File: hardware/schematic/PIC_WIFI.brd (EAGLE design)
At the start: 111.5 x 26.4 mm, 63 parts, among them J3 M40, J4 M40, J7 USB-A-S, Q1 8MHz, Q2 32.768KHz, U1 PIC32MX460F512L TQFP100, U2 3.3V, U3 5V

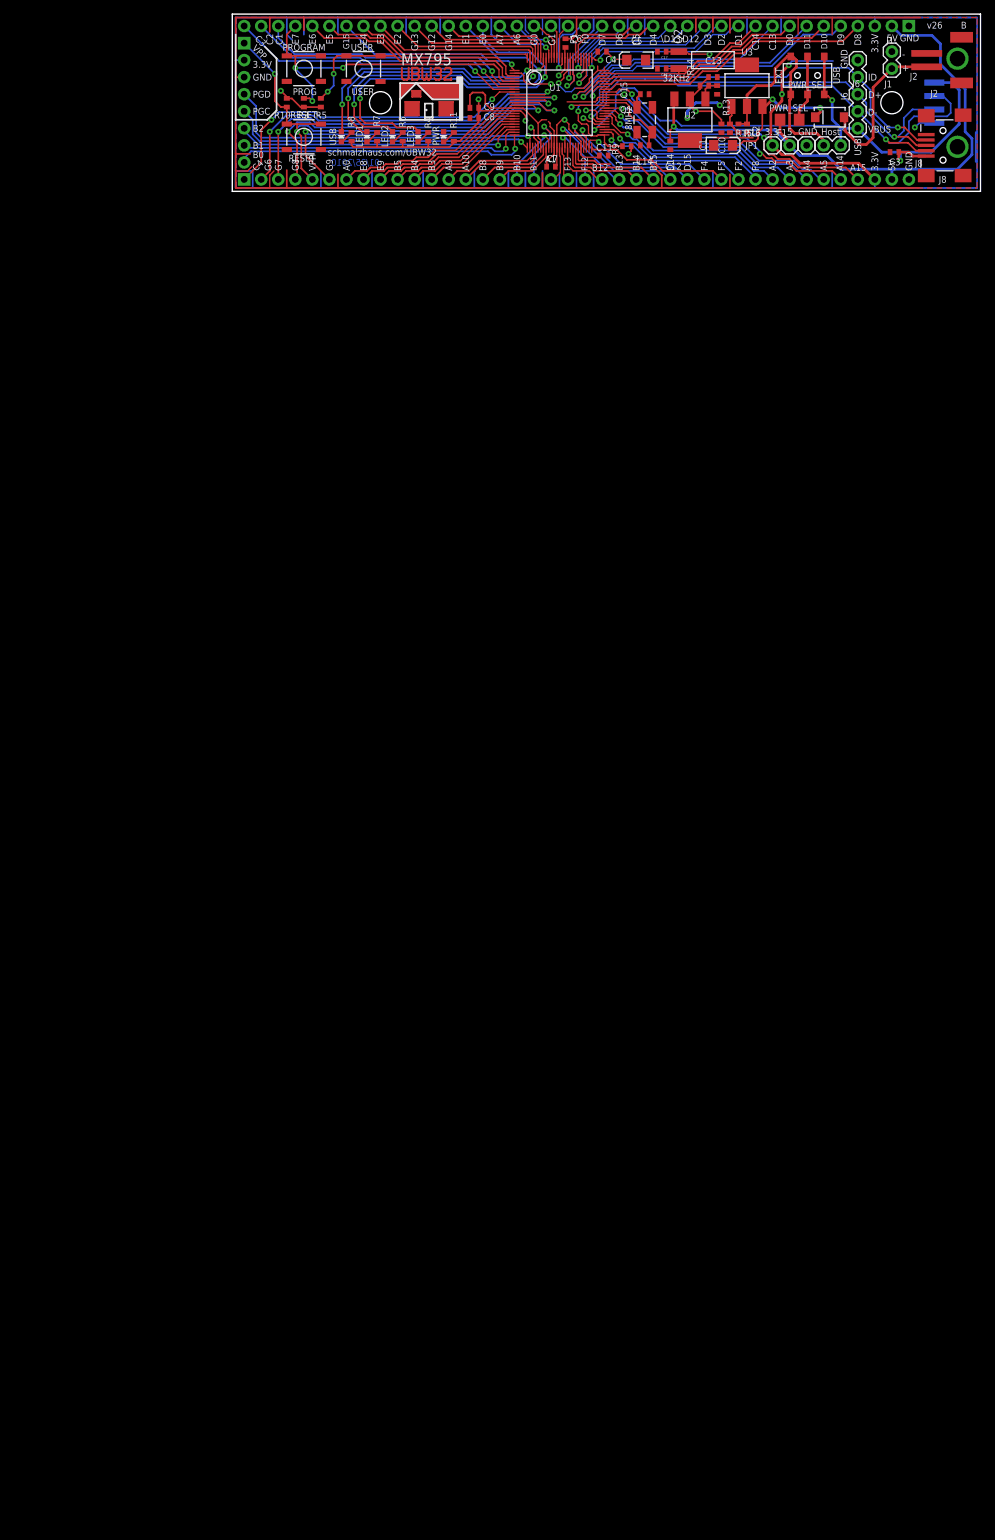
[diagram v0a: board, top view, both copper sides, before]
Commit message: First revision of dev board.  Fixed duplicate pin in waterworx.sch
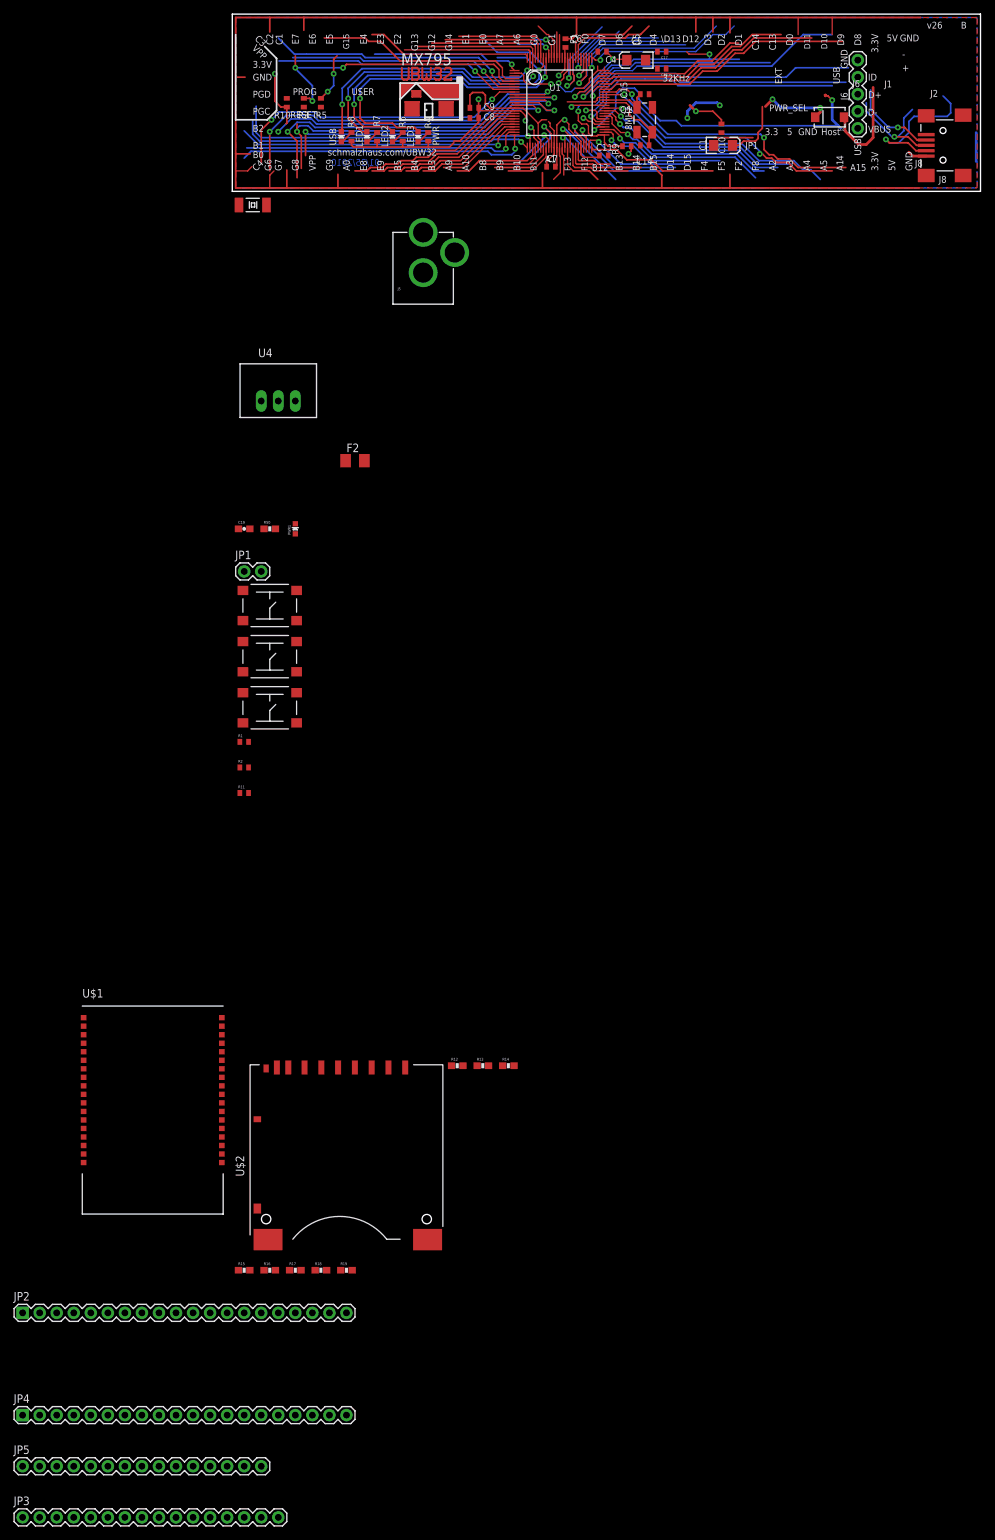
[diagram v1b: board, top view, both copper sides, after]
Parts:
- removed 3.3, 5, GND: M01PTH, SparkFun-12-01-09:1X01
- removed C12, C13: 1uF, SparkFun02-20-08:C0402
- removed C2, C3: 1uF, SparkFun:C0402
- removed F1: 250mA PTC Fuse, resistor:R1206
- removed J1: (no value), SparkFun-12-01-09:1X02
- removed J2: (no value), SparkFun:S2B-PH
- removed J3, J4: M40, SchmalzHaus:1X40
- removed J7: USB-A-S, SparkFun02-20-08:USB-A-S
- removed PROGRAM, USER: (no value), SparkFun02-20-08:TACTILE_SWITCH_SMD
- removed PWR: BLUE, SparkFun:LED-0603
- removed PWR_SEL: AYZ0202, SparkFun02-20-08:AYZ0202
- removed U$4: LOGO-SFENEW, SparkFun02-20-08:SFE-NEW-WEBLOGO
- removed U$6, U$7: STAND-OFF, SparkFun02-20-08:STAND-OFF
- removed U2: 3.3V, SparkFun:SOT223
- removed U3: 5V, SparkFun:SOT223
- added C19: 1uF, SparkFun-Passives:0603-CAP
- added F2: 500mA PTC Fuse, resistor:M1206
- added JP2, JP4: M20, SparkFun-Connectors:1X20
- added JP3: M16PTH, SparkFun-Connectors:1X16
- added JP5: M15, SparkFun-Connectors:1X15
- added PWR1: BLUE, SparkFun:LED-0603
- added R1, R2: 4.7K, SparkFun:C0402
- added R12, R17, R18, R19: 4.7K, SparkFun-Passives:0603-RES
- added R50: 330, SparkFun-Passives:0603-RES
- added U$1: MRF24WB0MA, lizardworx:SMD_MRF
- added U$2: SD_CARD_SOCKETALPS, lizardworx:SD_ALPS
- added U4: RECOM_X.X_REG78XX, lizardworx:RECOM
- added USER1, USER2: (no value), lizardworx:SWITCH-OMRON
- J5: value (none) -> POWER_JACKPTH; device SchmalzHaus:1X08 -> lizardworx:POWER_JACK_PTH
- JP1: device SparkFun-12-01-09:1X02 -> SparkFun-Connectors:1X02
- Q2: device SchmalzHaus:CRYSTAL-32KHZ-SMD -> lizardworx:CRYSTAL-SMD-4X2
- R10, R3, R5: value 10K -> 4.7K
- R11: value 330 -> 4.7K
- R13: value 390 -> 4.7K; device SparkFun:C0402 -> SparkFun-Passives:0603-RES
- R14, R16: value 240 -> 4.7K; device SparkFun:C0402 -> SparkFun-Passives:0603-RES
- R15: value 715 -> 4.7K; device SparkFun:C0402 -> SparkFun-Passives:0603-RES
- RESET: device SparkFun02-20-08:TACTILE_SWITCH_SMD -> lizardworx:SWITCH-OMRON
- moved R15 184.9 mm to (1.27, -161.3), turned to 0 degrees
- moved R16 184.0 mm to (5.08, -161.3), turned to 0 degrees
- moved R13 149.6 mm to (36.8, -130.8), turned to 0 degrees
- moved R14 148.9 mm to (40.6, -130.8)
- moved JP1 107.2 mm to (1.27, -57.1)
- moved R11 102.7 mm to (1.27, -90.2), turned to 0 degrees
- moved RESET 85.2 mm to (5.08, -77.5), turned to 0 degrees
- moved Q2 67.1 mm to (2.54, -2.54), turned to 0 degrees
- moved J5 49.7 mm to (27.9, -20.3), turned to 0 degrees
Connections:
- removed net 5V: 5.1, C12.1, F1.2, J3.2, J4.39, U2.3
- removed net 5V_ALT: C2.1, JP1.1, PWR_SEL.1, PWR_SEL.4, R16.1, U3.2
- removed net N$6: PWR.A, R11.1
- removed net RA3: J4.33, U1.59
- removed net RC4: J4.1, U1.9
- removed net RD0: J3.8, U1.72
- removed net RD10: J3.6, U1.70
- removed net RE8: J4.8, U1.18
- removed net RF0: J3.20, U1.87
- removed net RF1: J3.21, U1.88
- removed net RG12: J3.29, U1.96
- removed net RG13: J3.30, U1.97
- removed net RG14: J3.28, U1.95
- removed net RG6: J4.2, U1.10
- removed net RG7: J4.3, U1.11
- removed net RG8: J4.4, U1.12
- new net N$10: R18.1, R19.1
- new net N$19: PWR1.A, R50.1
- new net N$24: C19.1, F2.2, U4.VOUT
- new net N$5: R15.2, U$1.4
- new net SD_CD: JP2.9, U$2.CD, U1.96
- new net SD_CK: JP4.1, U$2.5, U1.10
- new net SD_CS: JP2.8, R18.2, U$2.1, U1.95
- new net SD_DI: JP4.3, U$2.2, U1.12
- new net SD_DO: JP4.2, U$2.7, U1.11
- new net SD_WP: JP2.10, U$2.WP, U1.97
- new net WF_CK: R13.1, U$1.34, U1.70
- new net WF_CS: U$1.23, U1.59
- new net WF_DI: R12.1, U$1.35, U1.72
- new net WF_DO: U$1.32, U1.9
- new net WF_HIBERNATE: U$1.20, U1.88
- new net WF_INT: R14.1, U$1.33, U1.18
- new net WF_RESET: R16.1, U$1.7, U1.87
- new net WF_WP: R17.2, U$1.16
- net 3.3V: now also F2.1, J6.2, JP3.2, JP5.14, R1.2, R12.2, R13.2, R14.2, R15.1, R16.2, R19.2, R2.2, R50.2, U$1.17, U$1.29, U$2.4; no longer 3.3.1, C13.1, J3.3, J4.38, J5.2, R10.1, R14.1, R3.1, R5.1, U2.2
- net D+: no longer J6.3, J7.D+
- net D-: no longer J6.2, J7.D-
- net GND: now also C19.2, J5.GND, J5.GNDBREAK, J6.3, JP1.2, JP3.1, JP5.15, PWR1.C, R17.1, U$1.1, U$1.10, U$1.18, U$1.19, U$1.25, U$1.28, U$1.30, U$1.36, U$2.12, U$2.3, U$2.6, U$2.VSS, U4.GND, USER1.1, USER1.2, USER2.1, USER2.2; no longer C12.2, C13.2, C2.2, C3.2, GND.1, J1.1, J2.1, J3.1, J4.40, J5.3, J6.5, J7.GND, PROGRAM.1, PROGRAM.2, PWR.C, R13.1, R15.1, USER.1, USER.2
- net N$1: now also R1.1, R10.1; no longer D1.A, J1.2, J2.2
- net N$2: now also D1.A, J5.PWR, JP1.1; no longer F1.1, PWR_SEL.2, PWR_SEL.5
- net N$3: now also R2.1, R5.1; no longer R13.2, R14.2, U2.1
- net N$4: now also R11.1, R3.1; no longer R15.2, R16.2, U3.1
- net PGC: now also J6.5; no longer J5.5
- net PGD: now also J6.4; no longer J5.4
- net RA0: now also JP4.5; no longer J4.7
- net RA1: now also JP4.16; no longer J4.19
- net RA10: now also JP4.11; no longer J4.14
- net RA14: now also JP5.12; no longer J4.36
- net RA15: now also JP5.13; no longer J4.37
- net RA2: now also JP5.9; no longer J4.32
- net RA4: now also JP5.10; no longer J4.34
- net RA5: now also JP5.11; no longer J4.35
- net RA6: now also JP2.4; no longer J3.24
- net RA7: now also JP2.5; no longer J3.25
- net RA9: now also JP4.10; no longer J4.13
- net RB0: no longer J5.8
- net RB1: no longer J5.7
- net RB10: now also JP4.14; no longer J4.17
- net RB11: now also JP4.15; no longer J4.18
- net RB12: now also JP4.19; no longer J4.22
- net RB13: now also JP4.20; no longer J4.23
- net RB14: now also JP5.1; no longer J4.24
- net RB15: now also JP5.2; no longer J4.25
- net RB2: no longer J5.6
- net RB3: now also JP4.9; no longer J4.12
- net RB4: now also JP4.8; no longer J4.11
- net RB5: now also JP4.7; no longer J4.10
- net RB8: now also JP4.12; no longer J4.15
- net RB9: now also JP4.13; no longer J4.16
- net RC1: now also JP2.18; no longer J3.38
- net RC13: now also JP3.6, Q2.P$2; no longer J3.9, Q2.X1
- net RC14: now also JP3.7, Q2.P$1; no longer J3.10, Q2.X2
- net RC2: now also JP2.19; no longer J3.39
- net RC3: now also JP2.20; no longer J3.40
- net RD1: now also JP3.8; no longer J3.11
- net RD11: now also JP3.5; no longer J3.7
- net RD12: now also JP3.11; no longer J3.14
- net RD13: now also JP3.12; no longer J3.15
- net RD14: now also JP5.3; no longer J4.26
- net RD15: now also JP5.4; no longer J4.27
- net RD2: now also JP3.9; no longer J3.12
- net RD3: now also JP3.10; no longer J3.13
- net RD4: now also JP3.13; no longer J3.16
- net RD5: now also JP3.14; no longer J3.17
- net RD6: now also JP3.15; no longer J3.18
- net RD7: now also JP2.1; no longer J3.19
- net RD8: now also JP3.3; no longer J3.4
- net RD9: now also JP3.4; no longer J3.5
- net RE0: now also JP2.6; no longer J3.26
- net RE1: now also JP2.7; no longer J3.27
- net RE2: now also JP2.11; no longer J3.31
- net RE3: now also JP2.12; no longer J3.32
- net RE4: now also JP2.13; no longer J3.33
- net RE5: now also JP2.15; no longer J3.35
- net RE6: now also JP2.16, USER2.3, USER2.4; no longer J3.36, USER.3, USER.4
- net RE7: now also JP2.17, USER1.3, USER1.4; no longer J3.37, PROGRAM.3, PROGRAM.4
- net RE9: now also JP4.6; no longer J4.9
- net RF12: now also JP4.18; no longer J4.21
- net RF13: now also JP4.17; no longer J4.20
- net RF2: now also JP5.7; no longer J4.30
- net RF4: now also JP5.5; no longer J4.28
- net RF5: now also JP5.6; no longer J4.29
- net RF8: now also JP5.8; no longer J4.31
- net RG0: now also JP2.3; no longer J3.23
- net RG1: now also JP2.2; no longer J3.22
- net RG15: now also JP2.14; no longer J3.34
- net RG9: now also JP4.4; no longer J4.6
- net USBID: no longer J6.4
- net VBUS: no longer C3.1, J6.1, J7.VBUS, JP1.2, PWR_SEL.3, PWR_SEL.6
- net VIN_RAW: now also U4.VIN; no longer U3.3
- net VPP: now also J6.1; no longer J4.5, J5.1
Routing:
- net 3.3V: track 486.2 -> 87.3 mm, vias 13 -> 10
- net 5V: track 87.3 -> 0.00 mm, vias 1 -> 0
- net RG6: track 57.3 -> 0.00 mm, vias 2 -> 0
- net RG7: track 56.9 -> 0.00 mm, vias 2 -> 0
- net SD_CK: track 0.00 -> 55.5 mm, vias 0 -> 2
- net RG8: track 54.6 -> 0.00 mm, vias 2 -> 0
- net SD_DI: track 0.00 -> 54.2 mm, vias 0 -> 2
- net SD_DO: track 0.00 -> 49.8 mm, vias 0 -> 2
- net RC4: track 49.1 -> 0.00 mm, vias 2 -> 0
- net WF_DO: track 0.00 -> 45.6 mm, vias 0 -> 2
- net VBUS: track 96.7 -> 53.7 mm, vias 3 -> 2
- net RD10: track 36.2 -> 0.00 mm
- net 5V_ALT: track 33.9 -> 0.00 mm
- net WF_CK: track 0.00 -> 33.7 mm
- net RA3: track 31.9 -> 0.00 mm, vias 1 -> 0
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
